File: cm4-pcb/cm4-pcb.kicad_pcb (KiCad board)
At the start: 2 copper layers, 16 x 18.5 mm, 9 parts, among them U1 Pfostenstecker_6_2x3, U2 Pfostenstecker_6_2x3, U3 Pfostenstecker_6_2x3, U4 MagJack-A70-112-331N126

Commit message: Ethernet
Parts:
- added C1: SMD-100nF, BohleBots:C0603, F.Cu at (95.7, 139.4)
- added H1: Pinhead_1x04V, BohleBots:HDR-TH_4P-P2.54-V-M-1, F.Cu at (91.8, 147.5)
- added H2: Pinhead_1x04V, BohleBots:HDR-TH_4P-P2.54-V-M-1, F.Cu at (91.8, 151.3)
- added J1: Conn_01x02_Pin, Connector_PinHeader_2.54mm:PinHeader_1x02_P2.54mm_Vertical, F.Cu at (92.4, 133.1)
- added J2: Conn_01x02_Pin, Connector_PinHeader_2.54mm:PinHeader_1x02_P2.54mm_Vertical, F.Cu at (97.0, 133.1)
- added LED1: LED_SMD, BohleBots:LED-SMD_L1.7-W0.6-RD, F.Cu at (91.9, 139.4)
- added LED2: LED_SMD, BohleBots:LED-SMD_L1.7-W0.6-RD, F.Cu at (91.9, 141.8)
- added R1: R, BohleBots:R_THT, F.Cu at (68.2, 155.8)
- added R2: R, BohleBots:R_THT, F.Cu at (68.2, 159.9)
- added R3: SMD-10k, BohleBots:R0603, F.Cu at (88.1, 132.1)
- added R4: SMD-220R, BohleBots:R0603, F.Cu at (88.1, 134.5)
- added R5: SMD-100R, BohleBots:R0603, F.Cu at (88.1, 137.0)
- added R6: SMD-100R, BohleBots:R0603, F.Cu at (88.1, 139.5)
- added R7: SMD-470R, BohleBots:R0603, F.Cu at (88.1, 142.0)
- added R8: SMD-470R, BohleBots:R0603, F.Cu at (88.1, 144.4)
- added U5: SMD-PUSH-BTN, BohleBots:SW-TH_5P-L6.0-W6.0-P4.50-LS6.5, F.Cu at (91.0, 157.9)
- moved U4 61.7 mm to (76.4, 142.1)
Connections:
- Module1 pad 10: unconnected-(Module1A-Ethernet_Pair0_N-Pad10) -> /TRD0_N
- Module1 pad 101: unconnected-(Module1B-USB_OTG_ID-Pad101) -> GND
- Module1 pad 103: unconnected-(Module1B-USB2_N-Pad103) -> USB_D-
- Module1 pad 105: unconnected-(Module1B-USB2_P-Pad105) -> USB_D+
- Module1 pad 11: unconnected-(Module1A-Ethernet_Pair2_P-Pad11) -> /TRD2_P
- Module1 pad 12: unconnected-(Module1A-Ethernet_Pair0_P-Pad12) -> /TRD0_P
- Module1 pad 13: GND -> Net-(Module1A-GND-Pad13)
- Module1 pad 14: GND -> Net-(Module1A-GND-Pad13)
- Module1 pad 15: unconnected-(Module1A-Ethernet_nLED3(3.3v)-Pad15) -> /ETH_LEDY
- Module1 pad 17: unconnected-(Module1A-Ethernet_nLED2(3.3v)-Pad17) -> /ETH_LEDG
- Module1 pad 21: unconnected-(Module1A-PI_nLED_Activity-Pad21) -> ACT_LED
- Module1 pad 28: unconnected-(Module1A-GPIO13-Pad28) -> P13
- Module1 pad 3: unconnected-(Module1A-Ethernet_Pair3_P-Pad3) -> /TRD3_P
- Module1 pad 30: unconnected-(Module1A-GPIO6-Pad30) -> SHUTDOWN
- Module1 pad 31: unconnected-(Module1A-GPIO12-Pad31) -> P12
- Module1 pad 34: unconnected-(Module1A-GPIO5-Pad34) -> SCL
- Module1 pad 4: unconnected-(Module1A-Ethernet_Pair1_P-Pad4) -> /TRD1_P
- Module1 pad 47: unconnected-(Module1A-GPIO23-Pad47) -> ESP-P23
- Module1 pad 5: unconnected-(Module1A-Ethernet_Pair3_N-Pad5) -> /TRD3_N
- Module1 pad 51: unconnected-(Module1A-GPIO15-Pad51) -> P15
- Module1 pad 54: unconnected-(Module1A-GPIO4-Pad54) -> SDA
- Module1 pad 55: unconnected-(Module1A-GPIO14-Pad55) -> P14
- Module1 pad 59: GND -> Net-(Module1A-GND-Pad59)
- Module1 pad 6: unconnected-(Module1A-Ethernet_Pair1_N-Pad6) -> /TRD1_N
- Module1 pad 60: GND -> Net-(Module1A-GND-Pad59)
- Module1 pad 65: GND -> Net-(Module1A-GND-Pad65)
- Module1 pad 66: GND -> Net-(Module1A-GND-Pad65)
- Module1 pad 78: unconnected-(Module1A-GPIO_VREF(1.8v/3.3v_Input)-Pad78) -> Net-(Module1A-GPIO_VREF(1.8v/3.3v_Input))
- Module1 pad 86: unconnected-(Module1A-+3.3v_(Output)-Pad86) -> Net-(Module1A-GPIO_VREF(1.8v/3.3v_Input))
- Module1 pad 9: unconnected-(Module1A-Ethernet_Pair2_N-Pad9) -> /TRD2_N
- Module1 pad 92: unconnected-(Module1A-RUN_PG-Pad92) -> RUN_PG
- Module1 pad 99: unconnected-(Module1A-Global_EN-Pad99) -> EN
- U1 pad 6: /ESP-P23 -> ESP-P23
- U2 pad 6: /ESP-P23 -> ESP-P23
- U3 pad 6: /ESP-P23 -> ESP-P23
- U4 pad 1: unconnected-(U4-TRD0+-Pad1) -> /TRD0_P
- U4 pad 10: unconnected-(U4-TRD3--Pad10) -> /TRD3_N
- U4 pad 11: unconnected-(U4-VC1-Pad11) -> /TR0_TAP
- U4 pad 12: unconnected-(U4-VC2-Pad12) -> /TR1_TAP
- U4 pad 13: unconnected-(U4-VC3-Pad13) -> /TR2_TAP
- U4 pad 14: unconnected-(U4-VC4-Pad14) -> /TR3_TAP
- U4 pad 15: unconnected-(U4-LEDG_A-Pad15) -> +3.3V
- U4 pad 16: unconnected-(U4-LEDG_K-Pad16) -> Net-(U4-LEDG_K)
- U4 pad 17: unconnected-(U4-LEDY_A-Pad17) -> +3.3V
- U4 pad 18: unconnected-(U4-LEDY_K-Pad18) -> Net-(U4-LEDY_K)
- U4 pad 19: unconnected-(U4-SHIELD-Pad19) -> GND
- U4 pad 2: unconnected-(U4-TRD0--Pad2) -> /TRD0_N
- U4 pad 20: unconnected-(U4-SHIELD-Pad20) -> GND
- U4 pad 3: unconnected-(U4-TRD1+-Pad3) -> /TRD1_P
- U4 pad 4: unconnected-(U4-CT-Pad4) -> Net-(C1-Pad2)
- U4 pad 5: unconnected-(U4-CT-Pad5) -> Net-(C1-Pad2)
- U4 pad 6: unconnected-(U4-TRD1--Pad6) -> /TRD1_N
- U4 pad 7: unconnected-(U4-TRD2+-Pad7) -> /TRD2_P
- U4 pad 8: unconnected-(U4-TRD2--Pad8) -> /TRD2_N
- U4 pad 9: unconnected-(U4-TRD3+-Pad9) -> /TRD3_P

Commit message: PCB Placement
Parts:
- removed IR-Connector1: ~, BohleBots:TASTER_LED
- removed LED1, LED2: LED_SMD, BohleBots:LED-SMD_L1.7-W0.6-RD
- removed U3: Pfostenstecker_6_2x3, BohleBots:HDR-TH_6P-P2.54-V-F-R2-C3-S2.54-4
- added ACT_LED1: LED_SMD, BohleBots:LED-SMD_L1.7-W0.6-RD, F.Cu at (36.0, 85.8)
- added C2: SMD-1uF, BohleBots:C0603, F.Cu at (-32.2, 76.2)
- added G***: LOGO, sarcat:sarcatLogoSmall, F.Cu at (58.8, 58.2)
- added G***: LOGO, sarcat:sarcatLabelSmall, F.Cu at (-54.8, 36.2)
- added G***: LOGO, BohleBots:logo_klein, F.Cu at (-47.2, 76.8)
- added G***: LOGO, sarcat:sarcatLogo, B.Cu at (-3.40, 60.4)
- added H3: MountingHole, BohleBots:MountingHole_4.3mm_M4, F.Cu at (-26.8, 64.7)
- added H4: MountingHole, BohleBots:MountingHole_4.3mm_M4, F.Cu at (26.8, 64.7)
- added H5: MountingHole, BohleBots:MountingHole_4.3mm_M4, F.Cu at (64.7, 26.8)
- added H6: MountingHole, BohleBots:MountingHole_4.3mm_M4, F.Cu at (-64.7, 26.8)
- added J3: USB1125-GF-B, USB1125-GF-B:USB1125GFB, F.Cu at (52.3, 45.9)
- added J4: Conn_02x03_Odd_Even, Connector_PinHeader_2.54mm:PinHeader_2x03_P2.54mm_Vertical, B.Cu at (1.27, 35.6)
- added RUN_LED1: LED_SMD, BohleBots:LED-SMD_L1.7-W0.6-RD, F.Cu at (48.0, 77.2)
- moved H2 183.2 mm to (-65.4, 57.3), turned to -90 degrees
- moved C1 179.7 mm to (-56.4, 43.6)
- moved Taster_LED2 170.7 mm to (-15.2, 81.6)
- moved Taster_LED1 170.4 mm to (15.2, 81.6)
- moved U4 153.6 mm to (-52.0, 57.8)
- moved R8 150.4 mm to (-43.0, 70.8), turned to 180 degrees
- moved R7 148.3 mm to (-43.0, 72.6), turned to 180 degrees
- moved U5 148.1 mm to (-37.3, 83.8), turned to -90 degrees
- moved R3 131.8 mm to (-32.2, 78.2)
- moved R2 103.8 mm to (38.2, 60.5), turned to 90 degrees
- moved R1 98.3 mm to (44.3, 60.5), turned to 90 degrees
- moved H1 96.8 mm to (41.0, 65.2), turned to 180 degrees
- moved J1 79.5 mm to (33.2, 80.0), turned to 90 degrees
- moved R6 76.7 mm to (33.4, 85.7), turned to 90 degrees
- moved J2 74.3 mm to (43.1, 82.0), turned to -90 degrees
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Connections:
- Module1 pad 13: Net-(Module1A-GND-Pad13) -> GND
- Module1 pad 14: Net-(Module1A-GND-Pad13) -> GND
- Module1 pad 59: Net-(Module1A-GND-Pad59) -> GND
- Module1 pad 60: Net-(Module1A-GND-Pad59) -> GND
- Module1 pad 65: Net-(Module1A-GND-Pad65) -> GND
- Module1 pad 66: Net-(Module1A-GND-Pad65) -> GND
- Module1 pad 84: unconnected-(Module1A-+3.3v_(Output)-Pad84) -> Net-(Module1A-GPIO_VREF(1.8v/3.3v_Input))
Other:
- board size 16 x 18.5 mm -> 140 x 70.5 mm
- board text added: "CM4 Power"
- board text added: "CPU Indicator LED"
- board text added: "RPI Activity LED"

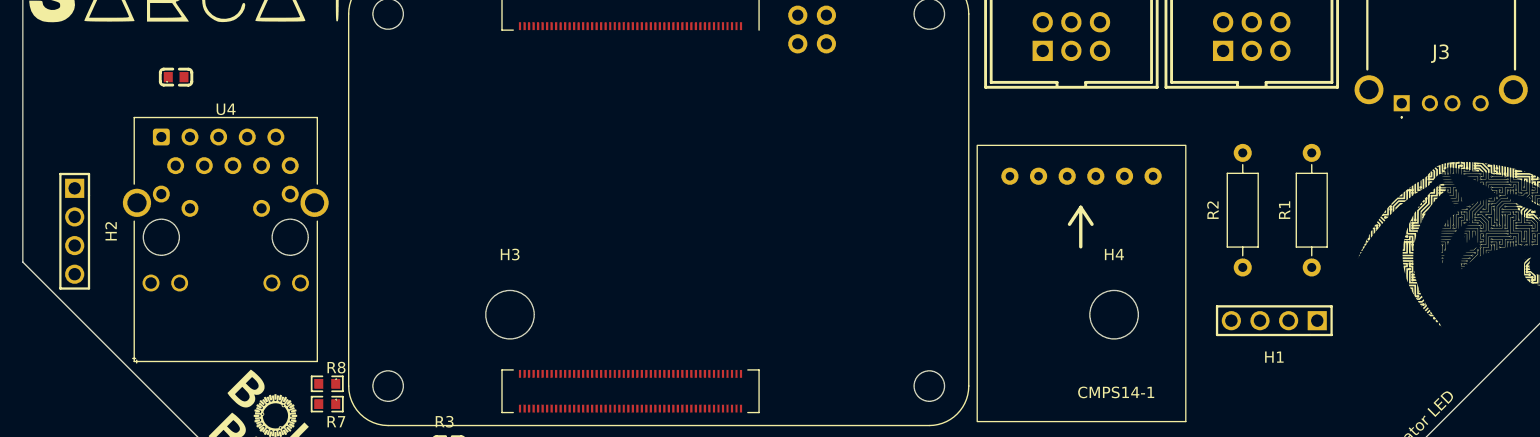
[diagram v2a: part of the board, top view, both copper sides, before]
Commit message: Added TVS Diodes
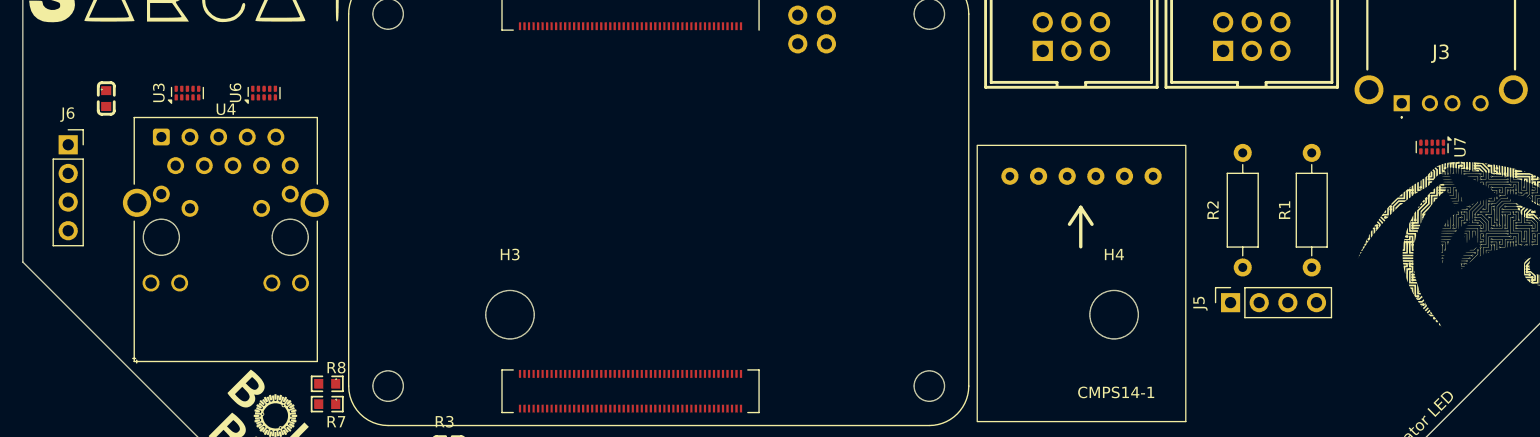
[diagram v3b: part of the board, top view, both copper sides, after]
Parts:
- removed H1, H2: Pinhead_1x04V, BohleBots:HDR-TH_4P-P2.54-V-M-1
- added J5: Conn_01x04, Connector_PinSocket_2.54mm:PinSocket_1x04_P2.54mm_Vertical, F.Cu at (37.1, 63.6)
- added J6: Conn_01x04, Connector_PinSocket_2.54mm:PinSocket_1x04_P2.54mm_Vertical, F.Cu at (-66.0, 49.6)
- added U3: TPD4EUSB30, Package_SON:USON-10_2.5x1.0mm_P0.5mm, F.Cu at (-55.4, 45.0)
- added U6: TPD4EUSB30, Package_SON:USON-10_2.5x1.0mm_P0.5mm, F.Cu at (-48.6, 45.0)
- added U7: TPD4EUSB30, Package_SON:USON-10_2.5x1.0mm_P0.5mm, F.Cu at (55.0, 49.8)
- moved C1 6.48 mm to (-62.6, 45.5), turned to -90 degrees

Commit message: V1.0
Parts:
- moved U7 5.83 mm to (49.8, 52.4), turned to 180 degrees
- moved U3 2.88 mm to (-56.6, 42.4)
- moved U6 2.60 mm to (-48.6, 42.4)
- moved G*** 1.08 mm to (58.4, 59.2)
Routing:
- net GND: track 0.00 -> 227.7 mm, vias 0 -> 21
- net +3.3V: track 0.00 -> 210.9 mm, vias 0 -> 1
- net SDA: track 0.00 -> 201.2 mm, vias 0 -> 2
- net SCL: track 0.00 -> 195.4 mm, vias 0 -> 3
- net +5V: track 0.00 -> 130.4 mm, vias 0 -> 3
- net /TRD0_N: track 0.00 -> 103.4 mm, vias 0 -> 2
- net /TRD0_P: track 0.00 -> 103.2 mm, vias 0 -> 2
- net ACT_LED: track 0.00 -> 96.6 mm, vias 0 -> 4
- net RUN_PG: track 0.00 -> 95.1 mm, vias 0 -> 3
- net EN: track 0.00 -> 89.0 mm, vias 0 -> 2
- net USB_D+: track 0.00 -> 87.5 mm
- net USB_D-: track 0.00 -> 87.5 mm
- net P14: track 0.00 -> 82.3 mm, vias 0 -> 2
- net P15: track 0.00 -> 79.1 mm, vias 0 -> 2
- net ESP-P23: track 0.00 -> 75.3 mm, vias 0 -> 1
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- added copper zone on B.Cu, net GND
- added copper zone on F.Cu, net GND

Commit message: V1.1
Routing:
- net GND: track 227.7 -> 231.0 mm, vias 21 -> 22
- net USB_D-: track 87.5 -> 88.2 mm
- net USB_D+: track 87.5 -> 88.3 mm
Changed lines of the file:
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@@
 	)
 	(segment
+		(start 50.17 52.4)
+		(end 48 52.4)
+		(width 0.25)
+		(layer "F.Cu")
+		(net 1)
+	)
+	(segment
 		(start -56.6 42.015)
 		(end -56.6 40.6)
@@
 	)
 	(segment
+		(start 50.17 52.4)
+		(end 49.4 52.4)
+		(width 0.25)
+		(layer "F.Cu")
+		(net 1)
+	)
+	(segment
 		(start -17.9 35.45)
 		(end -17.9 36)
@@
 	)
 	(segment
-		(start 50.17 52.4)
-		(end 49.4 52.4)
-		(width 0.2)
-		(layer "F.Cu")
-		(net 1)
-	)
-	(segment
 		(start -7.5 73)
 		(end -7.5 72.35)
@@
 	)
 	(segment
+		(start 48 52.4)
+		(end 47.2 53.2)
+		(width 0.25)
+		(layer "F.Cu")
+		(net 1)
+	)
+	(segment
 		(start -19.67 40.2)
 		(end -20.4 40.2)
@@
 	)
 	(via
+		(at 47.2 53.2)
+		(size 0.6)
+		(drill 0.3)
+		(layers "F.Cu" "B.Cu")
+		(net 1)
+	)
+	(via
 		(at 33 46.8)
 		(size 0.6)
@@
 	)
 	(segment
+		(start 49.399999 52.9)
+		(end 50.170001 52.9)
+		(width 0.25)
+		(layer "F.Cu")
+		(net 120)
+	)
+	(segment
 		(start 55.48 46.597)
 		(end 54.8 45.917)
@@
 		(layer "F.Cu")
 		(net 152)
+	)
+	(segment
+		(start 50.17 53.4)
+		(end 49.4 53.4)
+		(width 0.25)
+		(layer "F.Cu")
+		(net 152)

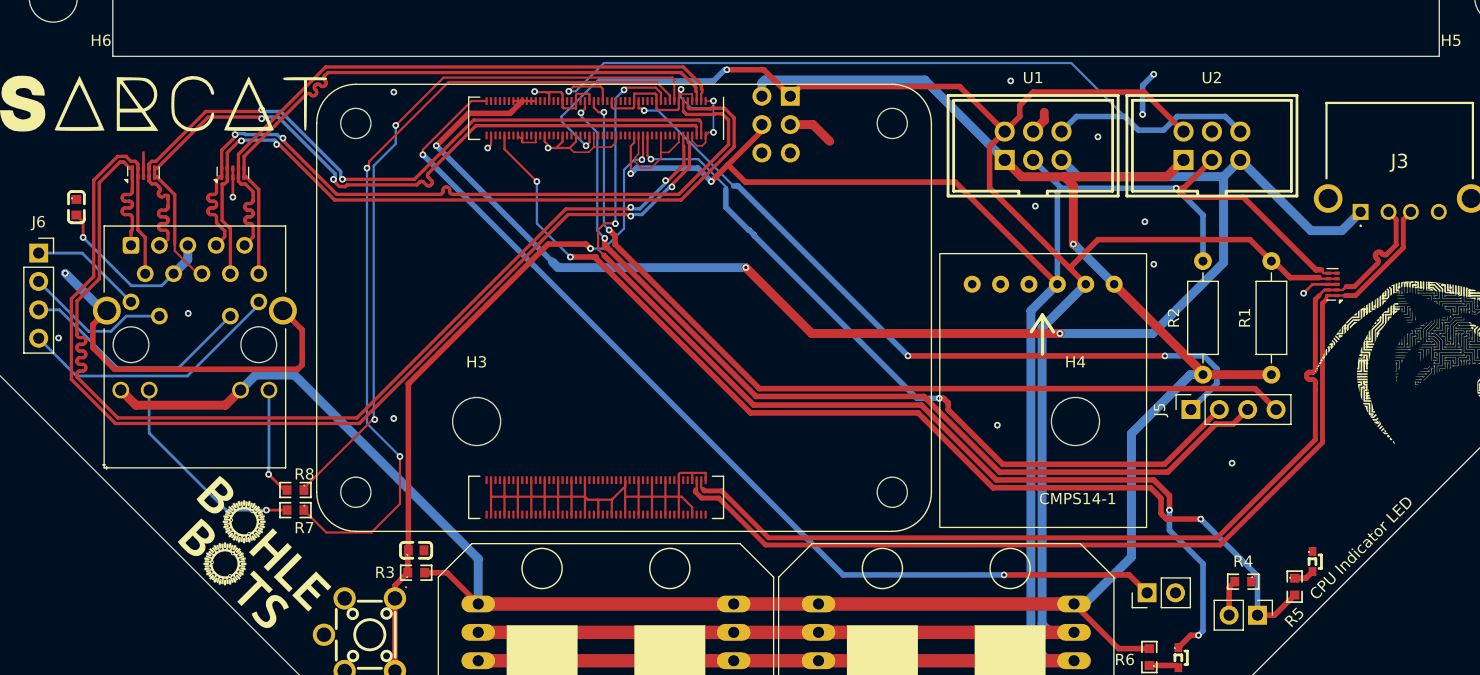
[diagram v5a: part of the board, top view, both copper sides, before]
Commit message: Added +5V Capacitors
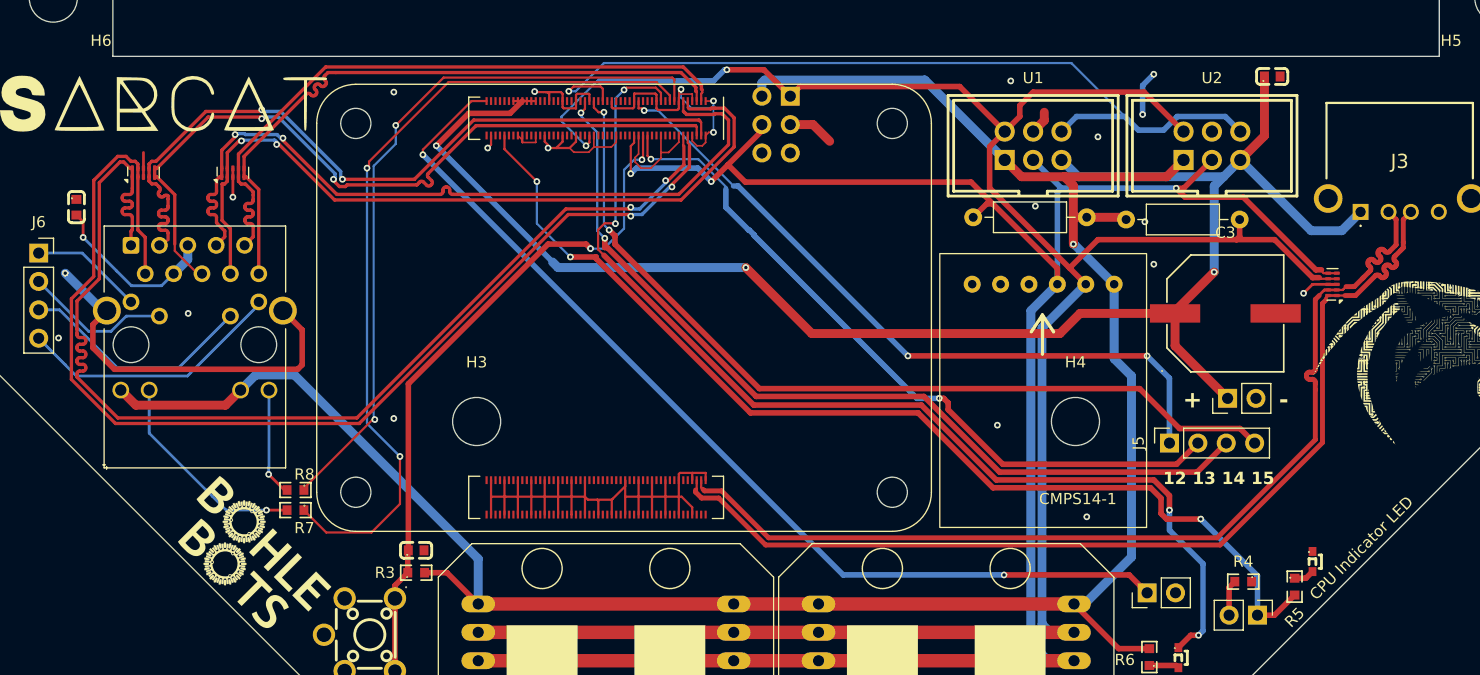
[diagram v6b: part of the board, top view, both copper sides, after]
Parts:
- added C3: SMD-680uF, BohleBots:CAP-SMD_BD10.0-L10.3-W10.3-LS11.3-FD, F.Cu at (40.2, 55.0)
- added C4: SMD-100nF, BohleBots:C0603, F.Cu at (44.4, 33.8)
- added J7: Conn_01x02, Connector_PinHeader_2.54mm:PinHeader_1x02_P2.54mm_Vertical, F.Cu at (40.4, 62.6)
- moved R1 19.0 mm to (31.3, 46.6), turned to 0 degrees
- moved R2 17.5 mm to (27.8, 46.4), turned to 180 degrees
- moved J5 3.56 mm to (35.2, 66.6)
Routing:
- net +5V: track 130.4 -> 148.4 mm
- net +3.3V: track 210.9 -> 203.7 mm
- net SCL: track 195.4 -> 190.9 mm
- net P13: track 67.9 -> 64.7 mm
- net P14: track 82.3 -> 79.1 mm
- net P12: track 66.9 -> 64.2 mm
- net SDA: track 201.2 -> 203.1 mm
- net USB_D+: track 88.3 -> 90.0 mm
- net USB_D-: track 88.2 -> 89.2 mm
- net P15: track 79.1 -> 78.5 mm
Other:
- board text added: "+"
- board text added: "-"
- board text added: "12 13 14 15"
